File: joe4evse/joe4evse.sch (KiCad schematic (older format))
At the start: 21 parts, among them J1 USB_B_Micro, J2 Conn_01x03, J3 Conn_01x03, J4 Conn_01x02, J5 Conn_01x02, J6 CONNFLY_Elec_DS1129-04-S8B0P-X, J7 8P8C_LED_Shielded, SW1 JS202011CQN, U1 CH340C, U2 MAX3485

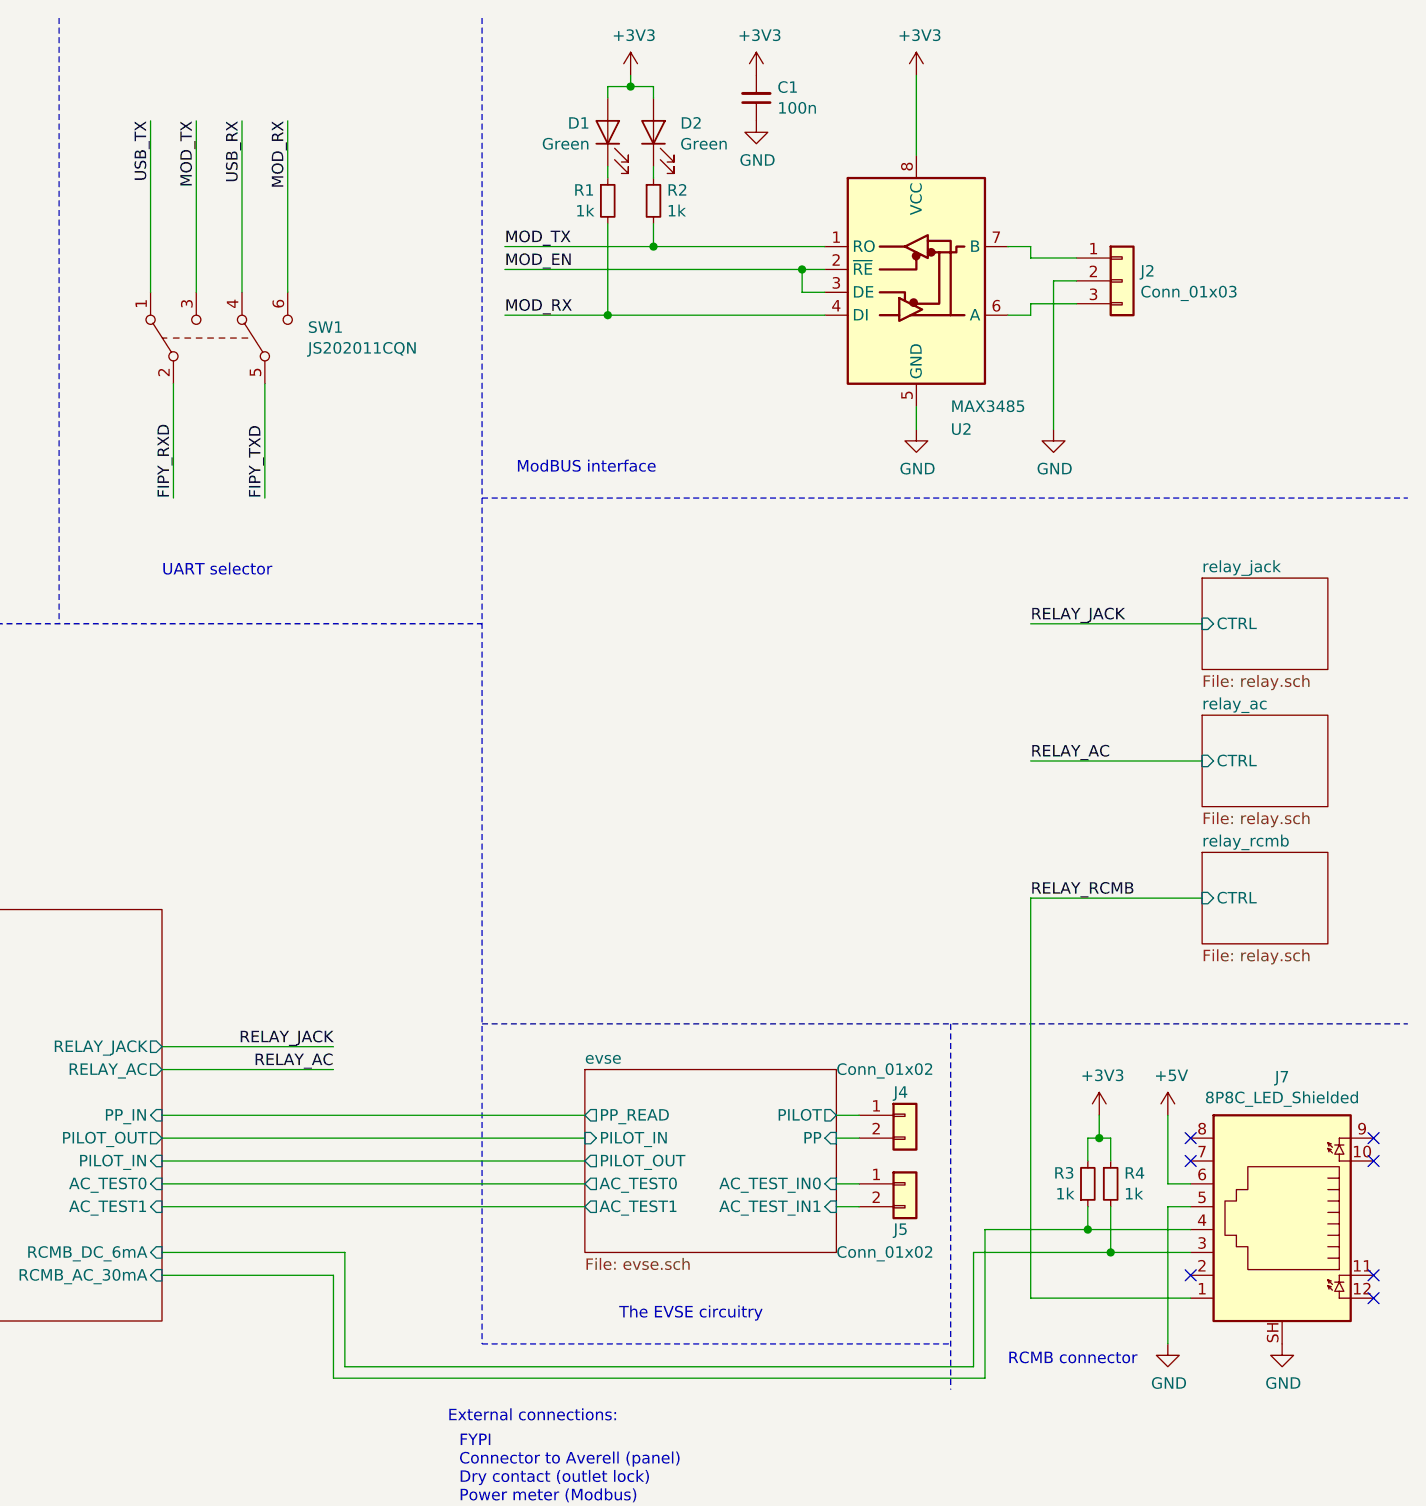
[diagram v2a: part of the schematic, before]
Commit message: joe/sch: Remove relays and only keep control circuitry
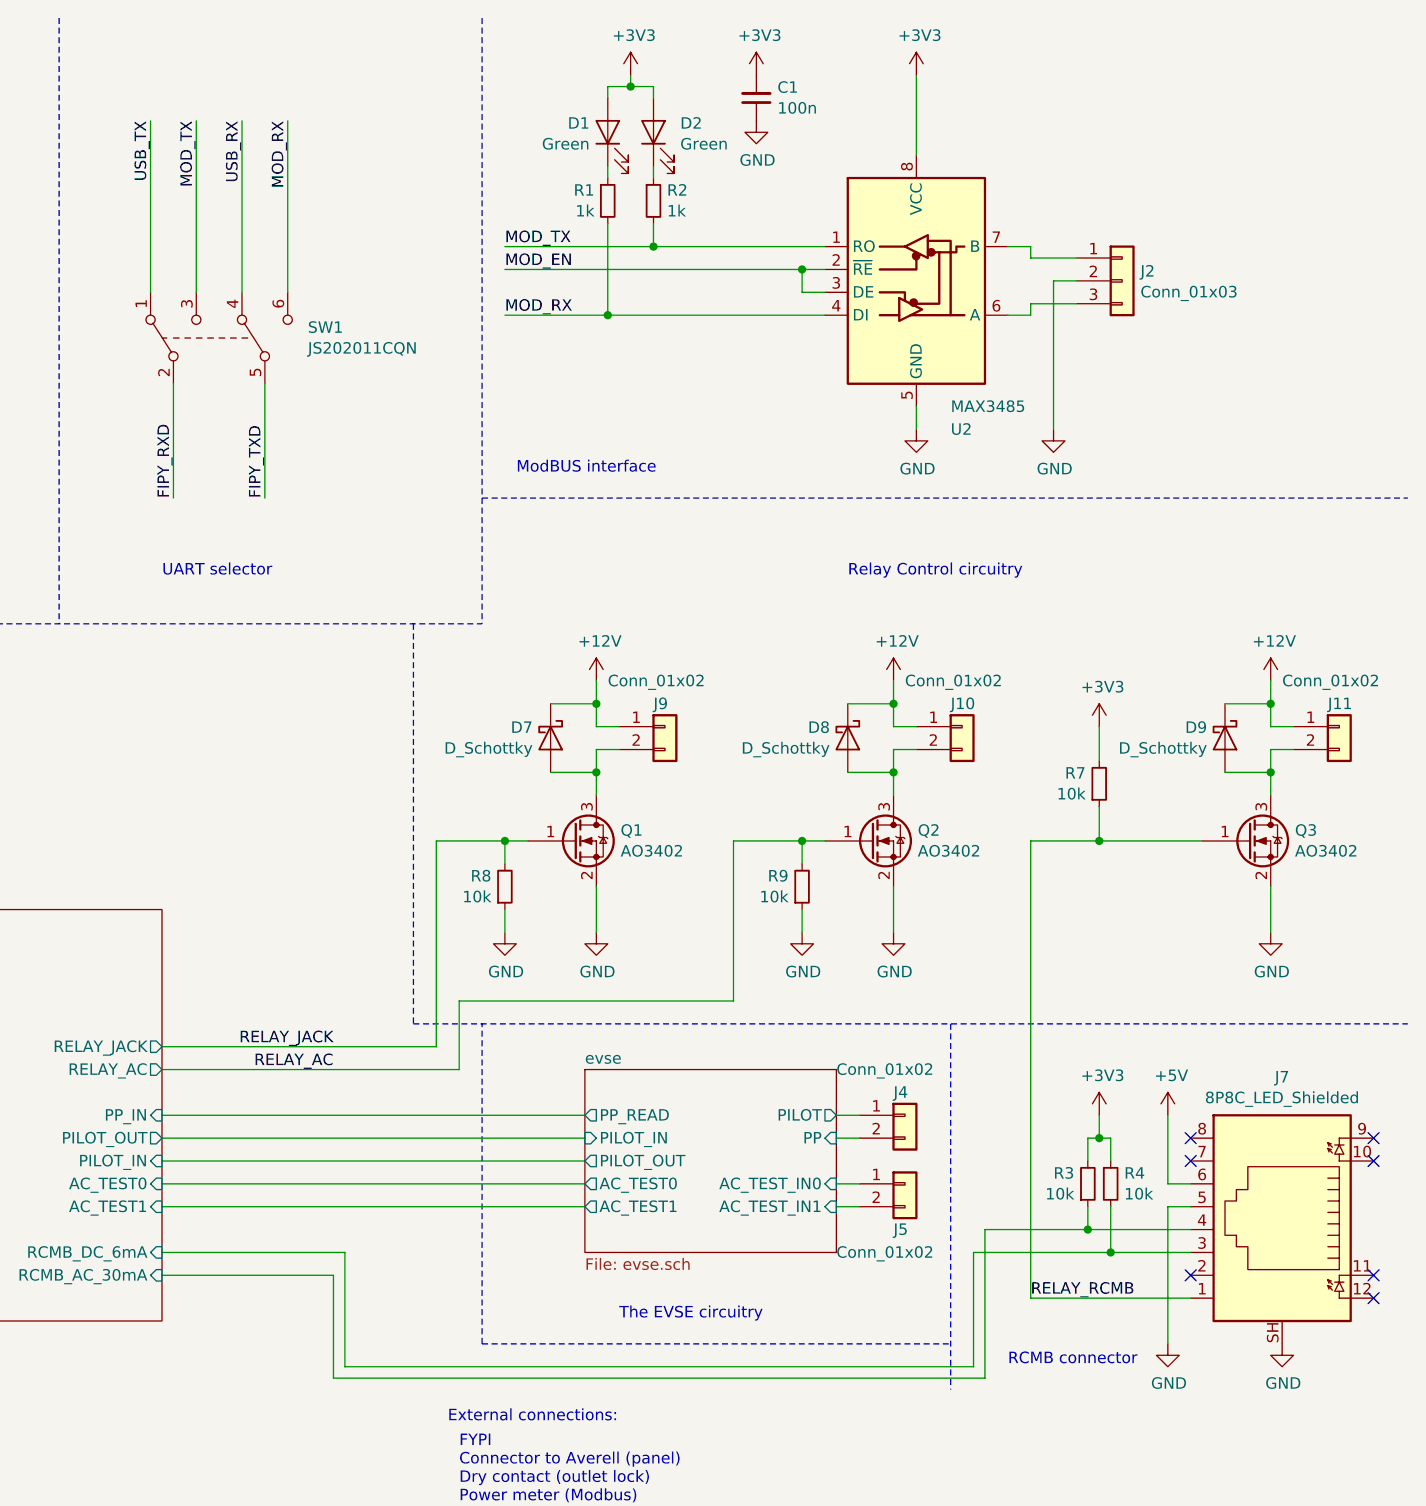
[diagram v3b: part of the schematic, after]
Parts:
- added D7, D8, D9: D_Schottky, Diode_SMD:D_SOD-123, symbol Device:D_Schottky
- added J10, J11, J9: Conn_01x02, Connector_JST:JST_PH_B2B-PH-K_1x02_P2.00mm_Vertical, symbol Connector_Generic:Conn_01x02
- added Q1, Q2, Q3: AO3402, Package_TO_SOT_SMD:SOT-23, symbol ma4evse:AO3402
- added R7, R8, R9: 10k, Resistor_SMD:R_0603_1608Metric, symbol Device:R_Small
- J3: footprint Connector_JST:JST_EH_S3B-EH_1x03_P2.50mm_Horizontal -> Connector_JST:JST_EH_B3B-EH-A_1x03_P2.50mm_Vertical
- R3, R4: value 1k -> 10k
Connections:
- net +12V: now also D7.1 (K), D8.1 (K), D9.1 (K), J10.1 (Pin_1), J11.1 (Pin_1), J9.1 (Pin_1)
- net +3V3: now also R7.2
- net GND: now also Q1.2 (S), Q2.2 (S), Q3.2 (S), R8.1, R9.1
- net RELAY_AC: now also Q2.1 (G), R9.2
- net RELAY_JACK: now also Q1.1 (G), R8.2
- net RELAY_RCMB: now also Q3.1 (G), R7.1
- new net: D8.2 (A), J10.2 (Pin_2), Q2.3 (D)
- new net: D9.2 (A), J11.2 (Pin_2), Q3.3 (D)
- new net: D7.2 (A), J9.2 (Pin_2), Q1.3 (D)
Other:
- note added: "Relay Control circuitry"

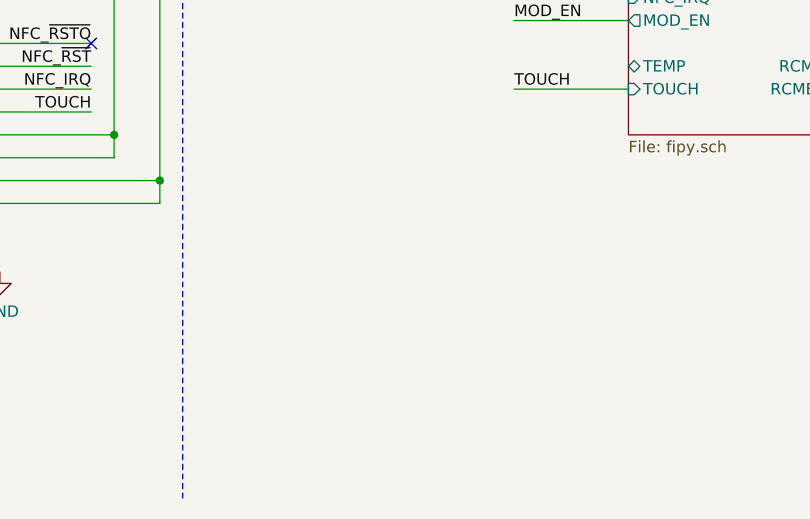
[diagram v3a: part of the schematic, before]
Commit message: joe/sch: Add mounting holes
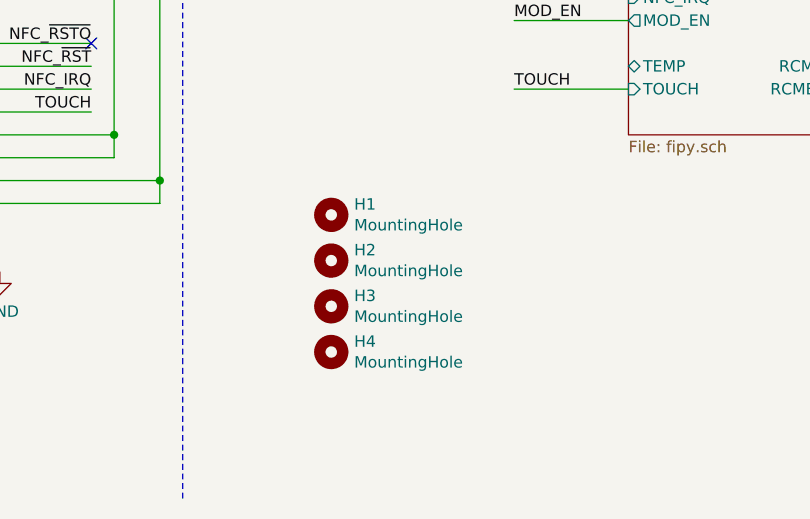
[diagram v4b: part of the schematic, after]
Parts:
- added H1, H2, H3, H4: MountingHole, MountingHole:MountingHole_3.2mm_M3_Pad_Via, symbol Mechanical:MountingHole
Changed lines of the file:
@@
 Text Notes 8750 2950 0    50   ~ 0
 Relay Control circuitry
+$Comp
+L Mechanical:MountingHole H1
+U 1 1 5E448D0E
+P 3200 6550
+F 0 "H1" H 3300 6596 50  0000 L CNN
+F 1 "MountingHole" H 3300 6505 50  0000 L CNN
+F 2 "MountingHole:MountingHole_3.2mm_M3_Pad_Via" H 3200 6550 50  0001 C CNN
+F 3 "~" H 3200 6550 50  0001 C CNN
+	1    3200 6550
+	1    0    0    -1
+$EndComp
+$Comp
+L Mechanical:MountingHole H2
+U 1 1 5E4499AD
+P 3200 6750
+F 0 "H2" H 3300 6796 50  0000 L CNN
+F 1 "MountingHole" H 3300 6705 50  0000 L CNN
+F 2 "MountingHole:MountingHole_3.2mm_M3_Pad_Via" H 3200 6750 50  0001 C CNN
+F 3 "~" H 3200 6750 50  0001 C CNN
+	1    3200 6750
+	1    0    0    -1
+$EndComp
+$Comp
+L Mechanical:MountingHole H3
+U 1 1 5E449BC8
+P 3200 6950
+F 0 "H3" H 3300 6996 50  0000 L CNN
+F 1 "MountingHole" H 3300 6905 50  0000 L CNN
+F 2 "MountingHole:MountingHole_3.2mm_M3_Pad_Via" H 3200 6950 50  0001 C CNN
+F 3 "~" H 3200 6950 50  0001 C CNN
+	1    3200 6950
+	1    0    0    -1
+$EndComp
+$Comp
+L Mechanical:MountingHole H4
+U 1 1 5E449F57
+P 3200 7150
+F 0 "H4" H 3300 7196 50  0000 L CNN
+F 1 "MountingHole" H 3300 7105 50  0000 L CNN
+F 2 "MountingHole:MountingHole_3.2mm_M3_Pad_Via" H 3200 7150 50  0001 C CNN
+F 3 "~" H 3200 7150 50  0001 C CNN
+	1    3200 7150
+	1    0    0    -1
+$EndComp
 $EndSCHEMATC

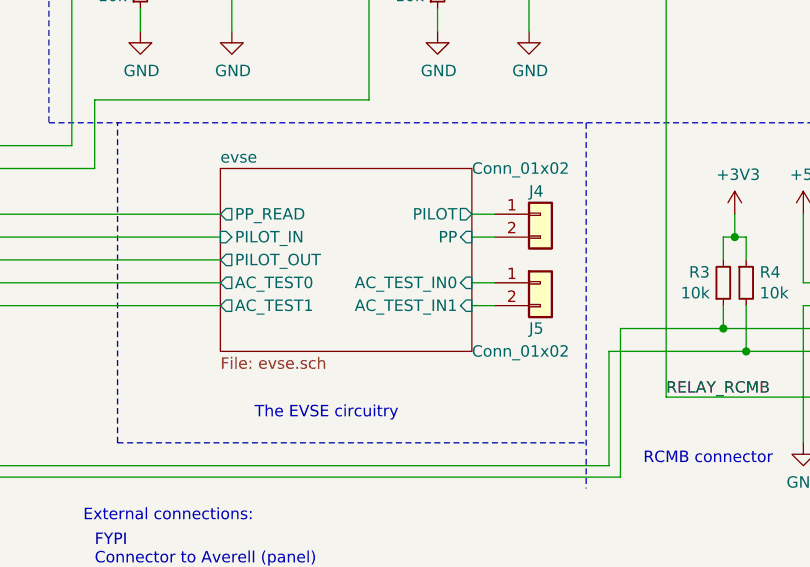
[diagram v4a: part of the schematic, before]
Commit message: joe/sch: Remove relays and reference AC test to neutral rather than GND
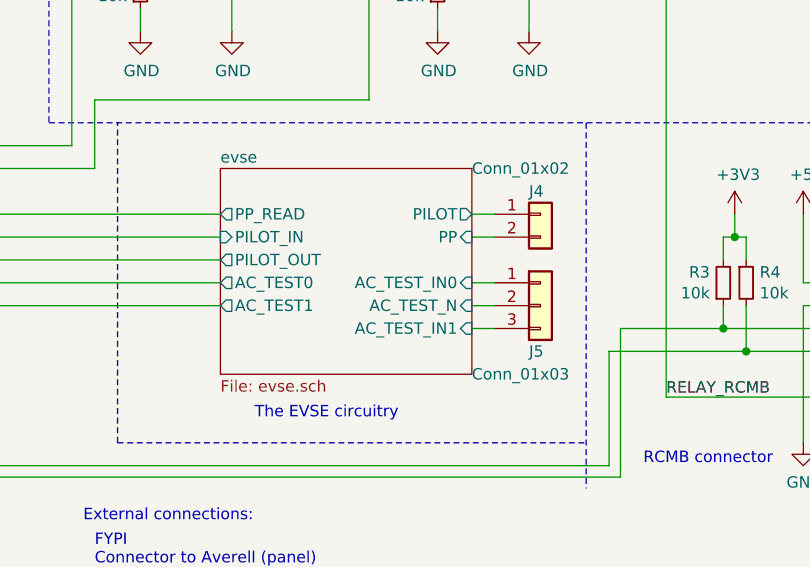
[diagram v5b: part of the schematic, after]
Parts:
- removed J5: Conn_01x02, Connector_JST:JST_NV_B02P-NV_1x02_P5.00mm_Vertical, symbol Connector_Generic:Conn_01x02
- added J5: Conn_01x03, Connector_JST:JST_NV_B03P-NV_1x03_P5.00mm_Vertical, symbol Connector_Generic:Conn_01x03
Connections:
- net evse/AC_TEST_IN0: now also J5.1 (Pin_1)
- net evse/AC_TEST_IN1: now also J5.3 (Pin_3)
- new net evse/AC_TEST_N: J5.2 (Pin_2)
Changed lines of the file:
@@
 RELAY_RCMB
-$Comp
-L Connector_Generic:Conn_01x02 J5
-U 1 1 5E01C3DF
-P 9000 5600
-F 0 "J5" H 8950 5400 50  0000 L CNN
-F 1 "Conn_01x02" H 8700 5300 50  0000 L CNN
-F 2 "Connector_JST:JST_NV_B02P-NV_1x02_P5.00mm_Vertical" H 9000 5600 50  0001 C CNN
-F 3 "~" H 9000 5600 50  0001 C CNN
-	1    9000 5600
-	1    0    0    -1
-$EndComp
 $Comp
 L Connector_Generic:Conn_01x02 J4
@@
 	8700 5300 8800 5300
 $Sheet
-S 7600 5100 1100 800
+S 7600 5100 1100 900
 U 5E2A7C72
 F0 "evse" 50
@@
 F4 "PILOT" O R 8700 5300 50
 F5 "AC_TEST_IN0" I R 8700 5600 50
-F6 "AC_TEST_IN1" I R 8700 5700 50
+F6 "AC_TEST_IN1" I R 8700 5800 50
 F7 "AC_TEST0" O L 7600 5600 50
 F8 "AC_TEST1" O L 7600 5700 50
 F9 "PP" I R 8700 5400 50
 F10 "PP_READ" O L 7600 5300 50
+F11 "AC_TEST_N" I R 8700 5700 50
 $EndSheet
 $Comp
@@
 	1    0    0    -1
 $EndComp
+$Comp
+L Connector_Generic:Conn_01x03 J5
+U 1 1 5E4D36EA
+P 9000 5700
+F 0 "J5" H 8950 5500 50  0000 L CNN
+F 1 "Conn_01x03" H 8700 5400 50  0000 L CNN
+F 2 "Connector_JST:JST_NV_B03P-NV_1x03_P5.00mm_Vertical" H 9000 5700 50  0001 C CNN
+F 3 "~" H 9000 5700 50  0001 C CNN
+	1    9000 5700
+	1    0    0    -1
+$EndComp
+Wire Wire Line
+	8700 5800 8800 5800
 $EndSCHEMATC

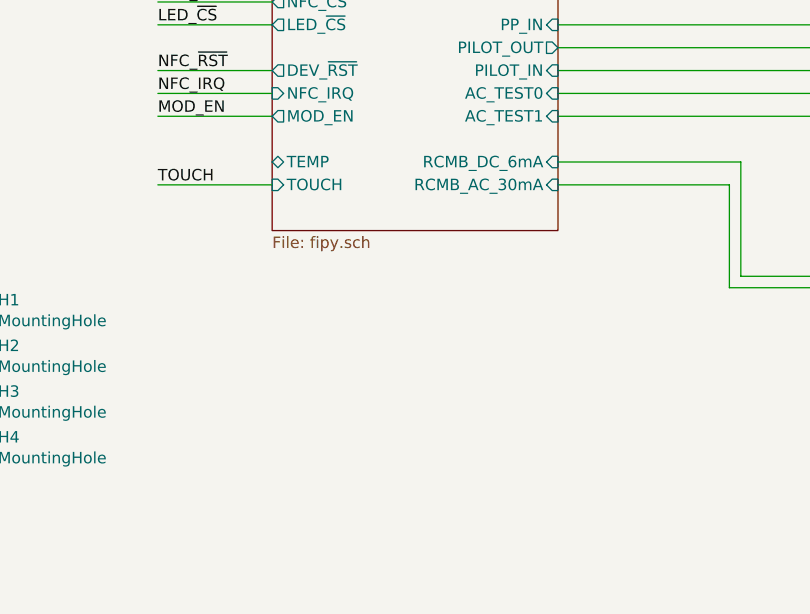
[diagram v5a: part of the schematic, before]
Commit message: joe/{sch, pcb}: Add missing temp sensor
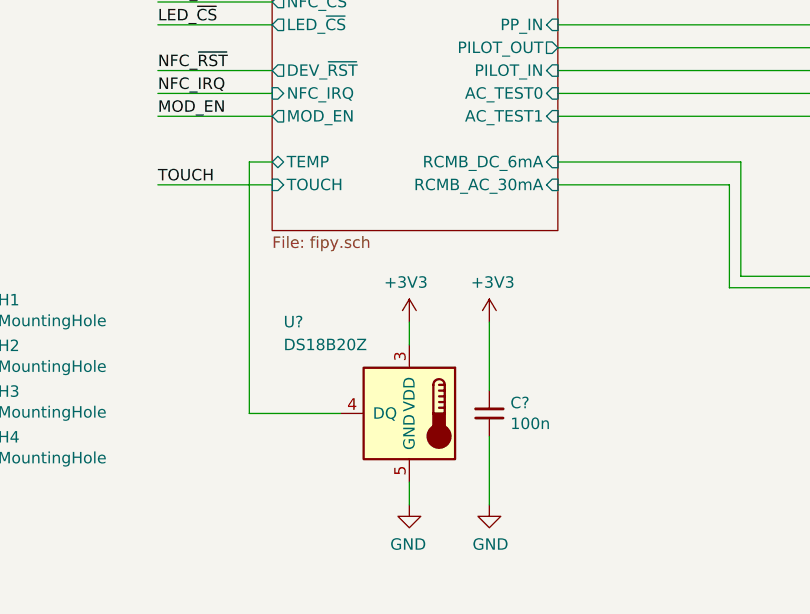
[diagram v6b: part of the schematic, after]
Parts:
- added C?: 100n, Capacitor_SMD:C_0603_1608Metric, symbol Device:C_Small
- added U?: DS18B20Z, Package_SO:SOIC-8_3.9x4.9mm_P1.27mm, symbol Sensor_Temperature:DS18B20Z
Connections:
- net +3V3: now also C?.2, U?.3 (VDD)
- net GND: now also C?.1, U?.5 (GND)
- net fipy/TEMP: now also U?.4 (DQ)
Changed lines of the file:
@@
 Wire Wire Line
 	8700 5800 8800 5800
+$Comp
+L Sensor_Temperature:DS18B20Z U?
+U 1 1 5E547938
+P 5100 7000
+F 0 "U?" H 5650 7400 50  0000 R CNN
+F 1 "DS18B20Z" H 5650 7300 50  0000 R CNN
+F 2 "Package_SO:SOIC-8_3.9x4.9mm_P1.27mm" H 4100 6750 50  0001 C CNN
+F 3 "http://datasheets.maximintegrated.com/en/ds/DS18B20.pdf" H 4950 7250 50  0001 C CNN
+	1    5100 7000
+	-1   0    0    -1
+$EndComp
+$Comp
+L power:+3V3 #PWR?
+U 1 1 5E54C87A
+P 5100 6600
+F 0 "#PWR?" H 5100 6450 50  0001 C CNN
+F 1 "+3V3" H 5115 6773 50  0000 C CNN
+F 2 "" H 5100 6600 50  0001 C CNN
+F 3 "" H 5100 6600 50  0001 C CNN
+	1    5100 6600
+	-1   0    0    -1
+$EndComp
+$Comp
+L power:GND #PWR?
+U 1 1 5E54D1CF
+P 5100 7400
+F 0 "#PWR?" H 5100 7150 50  0001 C CNN
+F 1 "GND" H 5105 7227 50  0000 C CNN
+F 2 "" H 5100 7400 50  0001 C CNN
+F 3 "" H 5100 7400 50  0001 C CNN
+	1    5100 7400
+	-1   0    0    -1
+$EndComp
+Wire Wire Line
+	4500 5900 4400 5900
+Wire Wire Line
+	4400 5900 4400 7000
+Wire Wire Line
+	4400 7000 4800 7000
+Wire Wire Line
+	5100 6600 5100 6700
+Wire Wire Line
+	5100 7400 5100 7300
+$Comp
+L Device:C_Small C?
+U 1 1 5E577814
+P 5450 7000
+F 0 "C?" H 5358 6954 50  0000 R CNN
+F 1 "100n" H 5358 7045 50  0000 R CNN
+F 2 "Capacitor_SMD:C_0603_1608Metric" H 5450 7000 50  0001 C CNN
+F 3 "~" H 5450 7000 50  0001 C CNN
+	1    5450 7000
+	-1   0    0    1
+$EndComp
+$Comp
+L power:+3V3 #PWR?
+U 1 1 5E57781A
+P 5450 6600
+F 0 "#PWR?" H 5450 6450 50  0001 C CNN
+F 1 "+3V3" H 5465 6773 50  0000 C CNN
+F 2 "" H 5450 6600 50  0001 C CNN
+F 3 "" H 5450 6600 50  0001 C CNN
+	1    5450 6600
+	1    0    0    -1
+$EndComp
+$Comp
+L power:GND #PWR?
+U 1 1 5E577820
+P 5450 7400
+F 0 "#PWR?" H 5450 7150 50  0001 C CNN
+F 1 "GND" H 5455 7227 50  0000 C CNN
+F 2 "" H 5450 7400 50  0001 C CNN
+F 3 "" H 5450 7400 50  0001 C CNN
+	1    5450 7400
+	1    0    0    -1
+$EndComp
+Wire Wire Line
+	5450 6600 5450 6900
+Wire Wire Line
+	5450 7100 5450 7400
 $EndSCHEMATC
